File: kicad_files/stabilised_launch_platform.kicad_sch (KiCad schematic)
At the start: 20 parts, among them J1 Conn_01x03_Male, J2 Conn_01x03_Male, J3 Conn_01x04_Male, SW1 SW_Push, U1 MAX7375AXR805, U2 AP7370-33Y, U3 STM32L011F3Px

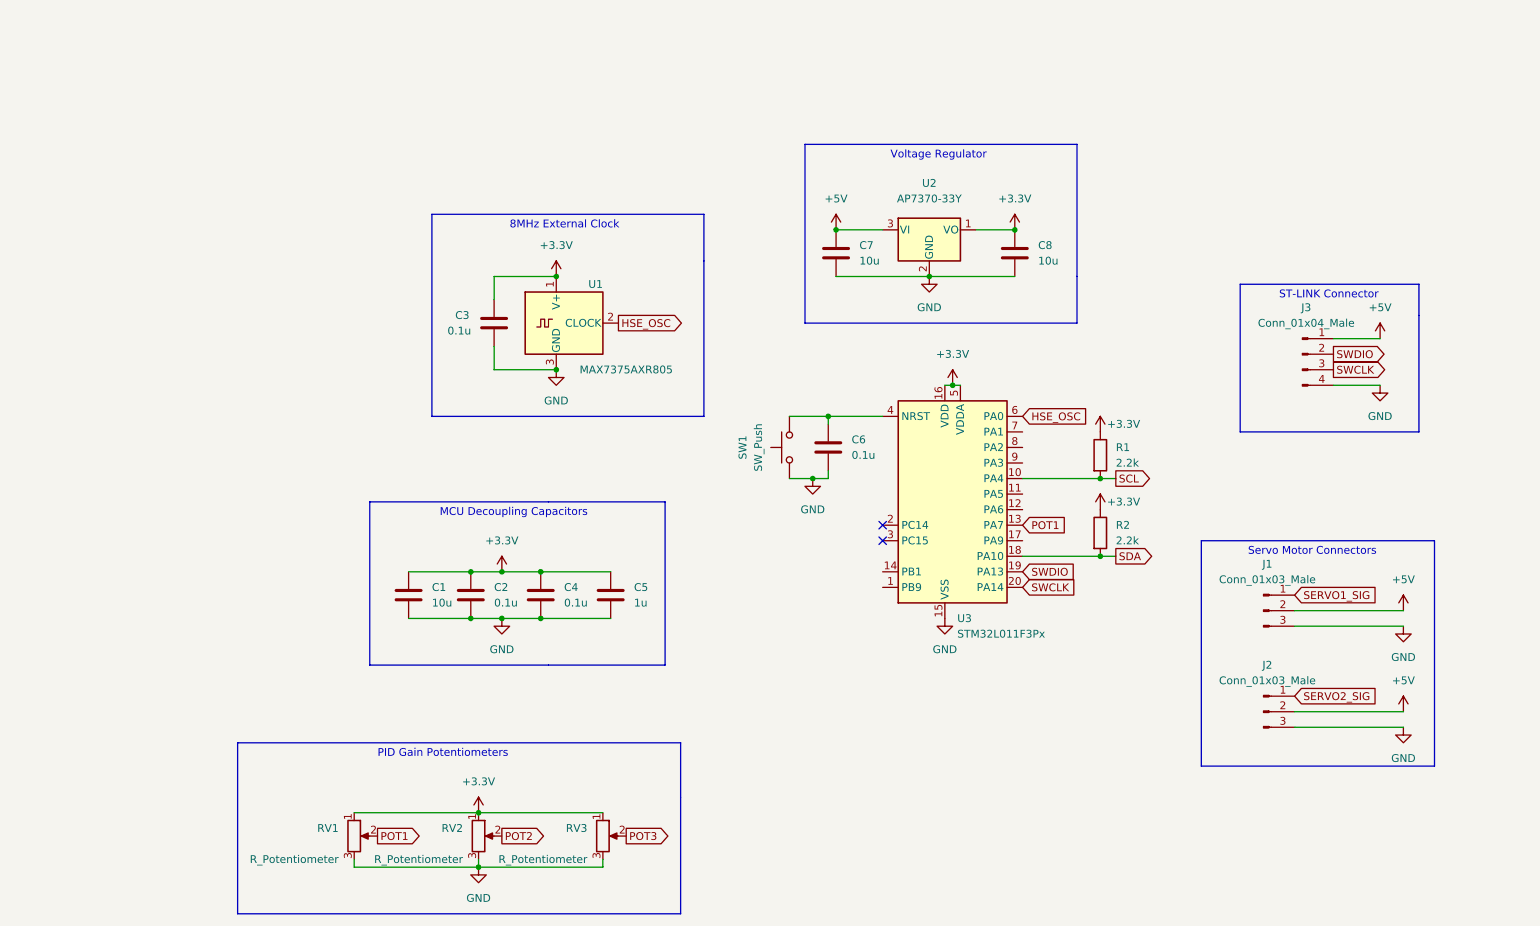
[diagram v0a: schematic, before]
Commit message: Added accelerometer and MOSFETs to schematic and PCB
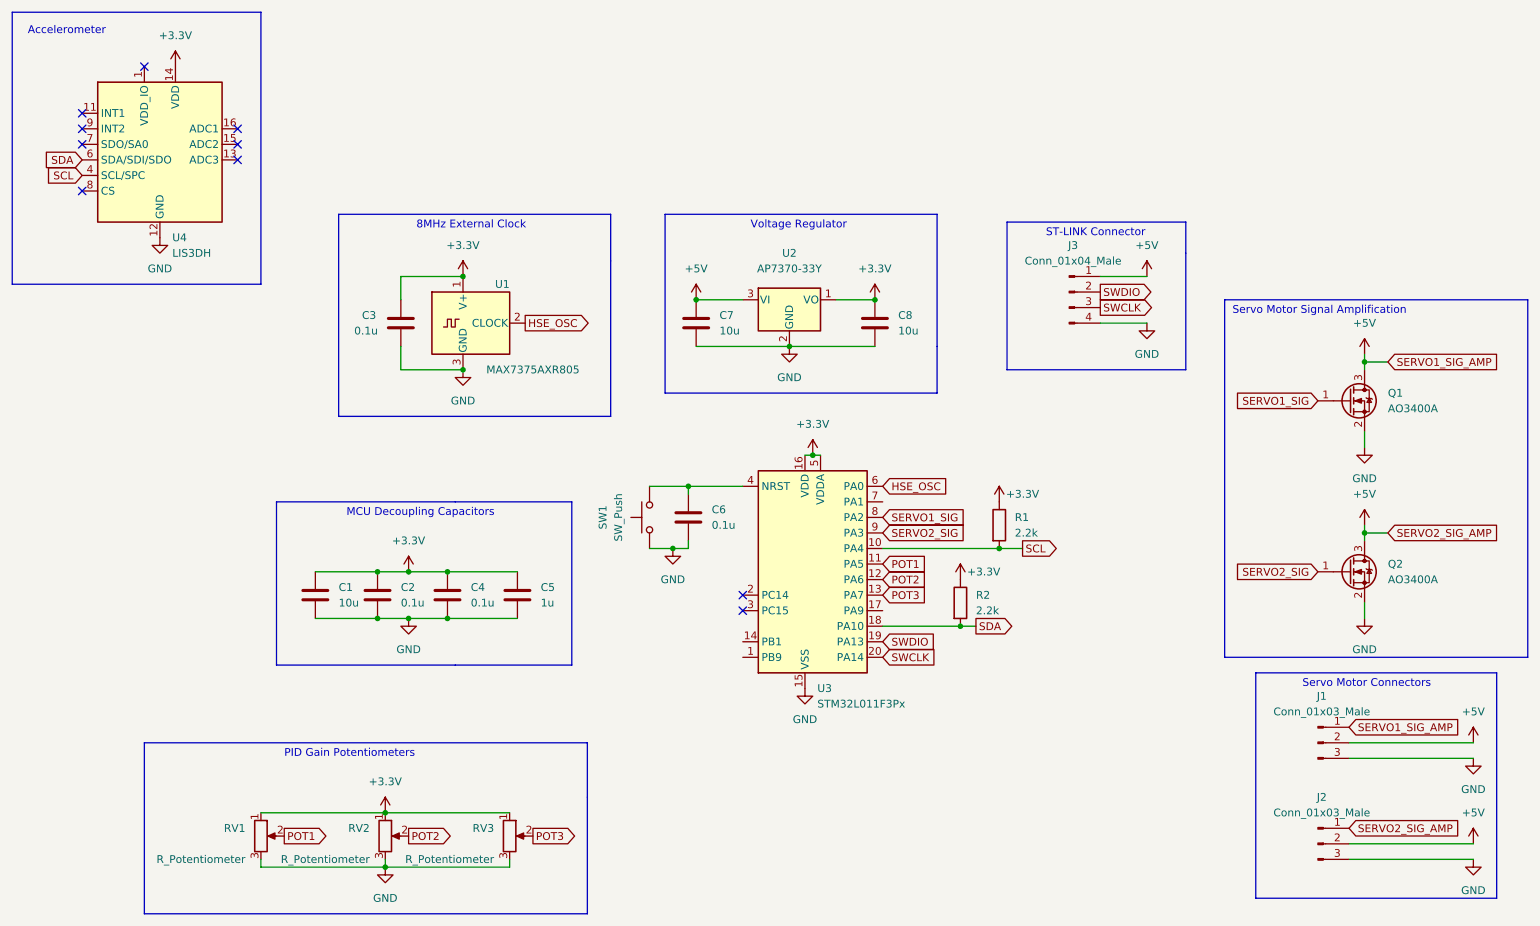
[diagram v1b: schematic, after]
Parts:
- added Q1, Q2: AO3400A, Package_TO_SOT_SMD:SOT-23, symbol Transistor_FET:AO3400A
- added U4: LIS3DH, Package_LGA:LGA-16_3x3mm_P0.5mm_LayoutBorder3x5y, symbol Sensor_Motion:LIS3DH
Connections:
- net +3.3V: now also U4.14 (VDD)
- net +5V: now also J1.1 (Pin_1), J2.1 (Pin_1), Q1.3 (D), Q2.3 (D)
- net GND: now also Q1.2 (S), Q2.2 (S), U4.10 (GND), U4.12 (GND), U4.5 (GND)
- net POT1: now also U3.11 (PA5); no longer U3.13 (PA7)
- net POT2: now also U3.12 (PA6)
- net POT3: now also U3.13 (PA7)
- net SCL: now also U4.4 (SCL/SPC)
- net SDA: now also U4.6 (SDA/SDI/SDO)
- net SERVO1_SIG: now also U3.8 (PA2), Q1.1 (G); no longer J1.1 (Pin_1)
- net SERVO2_SIG: now also U3.9 (PA3), Q2.1 (G); no longer J2.1 (Pin_1)
- no-connect marks 2 -> 10
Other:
- note added: "Accelerometer"
- note added: "Servo Motor Signal Amplification"
- moved on the sheet: C1, C2, C3, C4, C5, C6, C7, C8, J1, J2, J3, R1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
